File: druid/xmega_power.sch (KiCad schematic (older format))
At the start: 30 parts, among them U4 XC6206P332MR

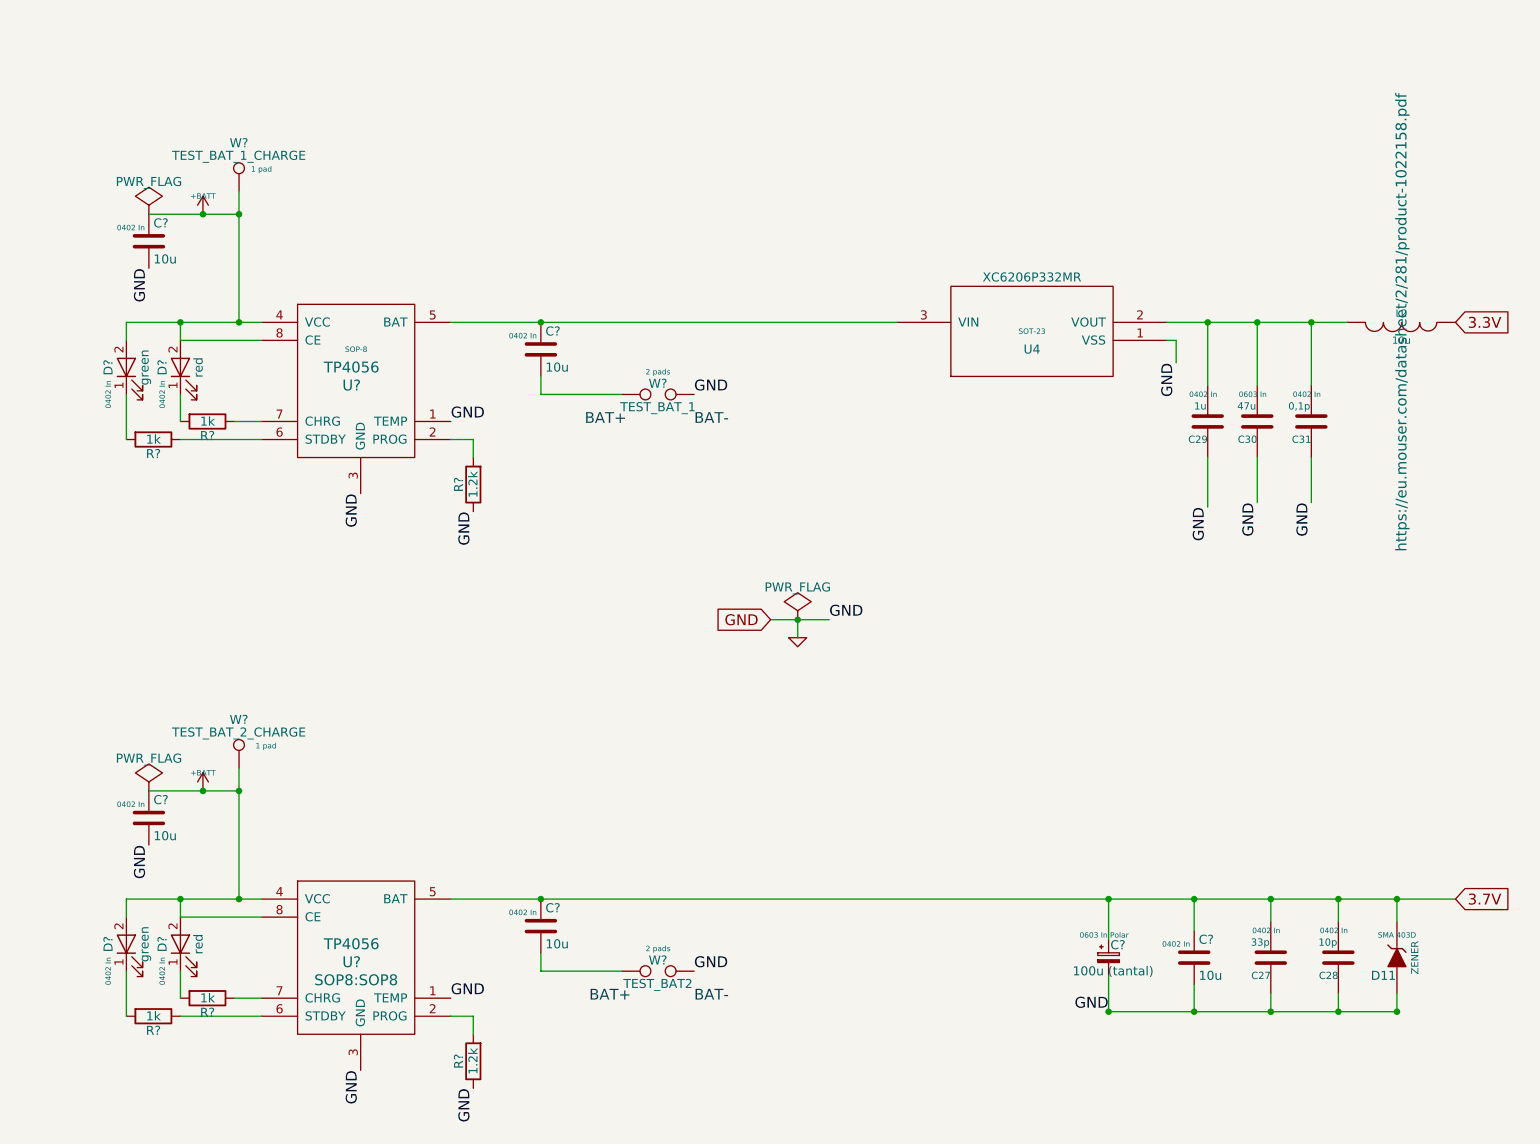
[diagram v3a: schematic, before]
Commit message: Add packages: power module completed. Add packages: keyboard module completed.
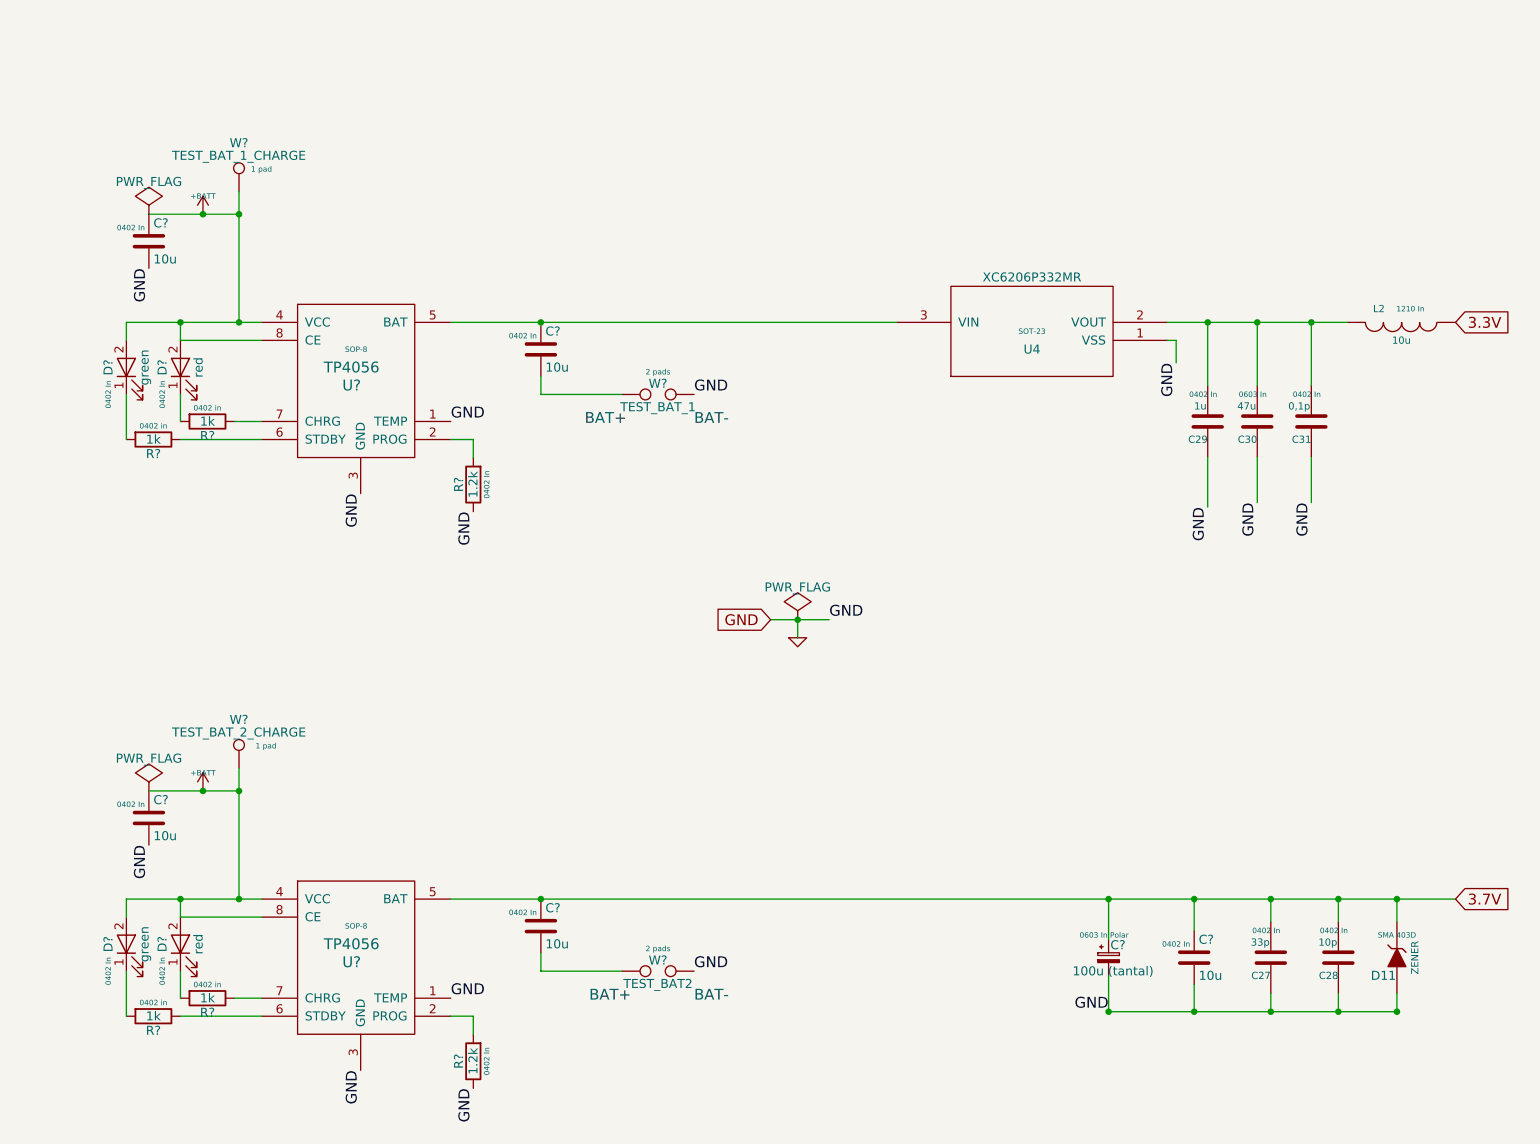
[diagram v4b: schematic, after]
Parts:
- removed R? (x3): 1k, symbol R
- removed R?: 1.2k, symbol R
- removed U?: TP4056, SOP8:SOP8, symbol TP4056
- added R? (x3): 1k, Resistors_SMD:R_0402, symbol R
- added R?: 1.2k, Resistors_SMD:R_0402, symbol R
- added U?: TP4056, SOP8:SOP8, symbol TP4056
- L2: footprint (none) -> inductor_1210_In:I_1210; case (none) -> 1210 In
- R?: footprint (none) -> Resistors_SMD:R_0402; case (none) -> 0402 in; example (none) -> https://eu.mouser.com/ProductDetail/Vishay/CRCW04021K00FKED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
- R?: footprint (none) -> Resistors_SMD:R_0402; case (none) -> 0402 In; example (none) -> https://eu.mouser.com/ProductDetail/Vishay/CRCW04021K20FKED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
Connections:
- net +BATT: now also U?.4 (VCC), U?.8 (CE)
- net 3.7V: now also U?.5 (BAT)
- net GND: now also R?.1, U?.1 (TEMP), U?.3 (GND)
- net at U?.7 (CHRG): now also R?.1
- net at D?.1 (K): now also R?.2 (x3)
- new net: R?.1, U?.6 (STDBY)
- new net: R?.1, U?.7 (CHRG)
- new net: R?.2, U?.2 (PROG)
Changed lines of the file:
@@
 U 1 1 5A9FD1C0
 P 9100 2050
-F 0 "L2" V 9050 2050 40  0000 C CNN
+F 0 "L2" V 9025 1925 40  0000 C CNN
 F 1 "10u" V 9200 2050 40  0000 C CNN
-F 2 "" H 9100 2050 60  0000 C CNN
-F 3 "https://eu.mouser.com/datasheet/2/281/product-1022158.pdf" H 9100 2050 60  0000 C CNN
+F 2 "inductor_1210_In:I_1210" H 9100 2050 60  0001 C CNN
+F 3 "https://eu.mouser.com/datasheet/2/281/product-1022158.pdf" H 9100 2050 60  0001 C CNN
 F 4 "https://eu.mouser.com/ProductDetail/Murata-Electronics/1276AS-H-100M%3dP2?qs=sGAEpiMZZMsg%252by3WlYCkUwoncuxJKc7T%2ffTlu7eSjNI%3d" V 9100 2050 60  0001 C CNN "example"
+F 5 "1210 In" V 9025 2100 30  0000 C CNN "case"
 	1    9100 2050
 	0    1    1    0
@@
 $Comp
 L R R?
-U 1 1 5C6AAFC7
-P 2475 2600
-F 0 "R?" V 2555 2600 50  0000 C CNN
-F 1 "1k" V 2475 2600 50  0000 C CNN
-F 2 "" V 2405 2600 50  0000 C CNN
-F 3 "" H 2475 2600 50  0000 C CNN
-	1    2475 2600
-	0    1    1    0
-$EndComp
-$Comp
-L R R?
 U 1 1 5C6AB0B6
 P 2175 2700
 F 0 "R?" V 2255 2700 50  0000 C CNN
 F 1 "1k" V 2175 2700 50  0000 C CNN
-F 2 "" V 2105 2700 50  0000 C CNN
-F 3 "" H 2175 2700 50  0000 C CNN
+F 2 "Resistors_SMD:R_0402" V 2105 2700 50  0001 C CNN
+F 3 "https://eu.mouser.com/datasheet/2/427/crcwce3-1223726.pdf" H 2175 2700 50  0001 C CNN
+F 4 "https://eu.mouser.com/ProductDetail/Vishay/CRCW04021K00FKEDC?qs=sGAEpiMZZMtlubZbdhIBIIZe04wfiaJWtbhT4BxhiTc%3d" V 2175 2700 60  0001 C CNN "example"
+F 5 "0402 in" V 2100 2700 30  0000 C CNN "case"
 	1    2175 2700
 	0    1    1    0
@@
 F 0 "R?" V 4030 2950 50  0000 C CNN
 F 1 "1.2k" V 3950 2950 50  0000 C CNN
-F 2 "" V 3880 2950 50  0000 C CNN
-F 3 "" H 3950 2950 50  0000 C CNN
+F 2 "Resistors_SMD:R_0402" V 3880 2950 50  0001 C CNN
+F 3 "https://eu.mouser.com/datasheet/2/427/crcwce3-1223726.pdf" H 3950 2950 50  0001 C CNN
+F 4 "https://eu.mouser.com/ProductDetail/Vishay/CRCW04021K20FKEDC?qs=sGAEpiMZZMtlubZbdhIBIIZe04wfiaJWRBT%2frAKZHAM%3d" V 3950 2950 60  0001 C CNN "example"
+F 5 "0402 In" V 3875 2950 30  0000 C CNN "case"
 	1    3950 2950
 	-1   0    0    1
@@
 $EndComp
 Connection ~ 4325 5250
-$Comp
-L TP4056 U?
-U 1 1 5C6B090F
-P 3325 5450
-F 0 "U?" H 3275 5300 60  0000 C CNN
-F 1 "TP4056" H 3275 5400 60  0000 C CNN
-F 2 "SOP8:SOP8" H 3300 5200 60  0000 C CNN
-F 3 "" H 3375 5450 60  0000 C CNN
-	1    3325 5450
-	1    0    0    -1
-$EndComp
 Text Label 3825 5800 0    60   ~ 0
 GND
@@
 Text Notes 4825 5825 2    60   ~ 0
 BAT+\n
-$Comp
-L R R?
-U 1 1 5C6B092E
-P 2475 5800
-F 0 "R?" V 2555 5800 50  0000 C CNN
-F 1 "1k" V 2475 5800 50  0000 C CNN
-F 2 "" V 2405 5800 50  0000 C CNN
-F 3 "" H 2475 5800 50  0000 C CNN
-	1    2475 5800
-	0    1    1    0
-$EndComp
-$Comp
-L R R?
-U 1 1 5C6B0934
-P 2175 5900
-F 0 "R?" V 2255 5900 50  0000 C CNN
-F 1 "1k" V 2175 5900 50  0000 C CNN
-F 2 "" V 2105 5900 50  0000 C CNN
-F 3 "" H 2175 5900 50  0000 C CNN
-	1    2175 5900
-	0    1    1    0
-$EndComp
 Wire Wire Line
 	2325 5350 2775 5350
@@
 Text Label 3325 6200 3    60   ~ 0
 GND
-$Comp
-L R R?
-U 1 1 5C6B095B
-P 3950 6150
-F 0 "R?" V 4030 6150 50  0000 C CNN
-F 1 "1.2k" V 3950 6150 50  0000 C CNN
-F 2 "" V 3880 6150 50  0000 C CNN
-F 3 "" H 3950 6150 50  0000 C CNN
-	1    3950 6150
-	-1   0    0    1
-$EndComp
 Text Label 3950 6300 3    60   ~ 0
 GND
@@
 	1    0    0    -1
 $EndComp
+$Comp
+L R R?
+U 1 1 5C6E4482
+P 2475 2600
+F 0 "R?" V 2555 2600 50  0000 C CNN
+F 1 "1k" V 2475 2600 50  0000 C CNN
+F 2 "Resistors_SMD:R_0402" V 2405 2600 50  0001 C CNN
+F 3 "https://eu.mouser.com/datasheet/2/427/crcwce3-1223726.pdf" H 2475 2600 50  0001 C CNN
+F 4 "https://eu.mouser.com/ProductDetail/Vishay/CRCW04021K00FKEDC?qs=sGAEpiMZZMtlubZbdhIBIIZe04wfiaJWtbhT4BxhiTc%3d" V 2475 2600 60  0001 C CNN "example"
+F 5 "0402 in" V 2400 2600 30  0000 C CNN "case"
+	1    2475 2600
+	0    1    1    0
+$EndComp
+$Comp
+L R R?
+U 1 1 5C6E463E
+P 2175 5900
+F 0 "R?" V 2255 5900 50  0000 C CNN
+F 1 "1k" V 2175 5900 50  0000 C CNN
+F 2 "Resistors_SMD:R_0402" V 2105 5900 50  0001 C CNN
+F 3 "https://eu.mouser.com/datasheet/2/427/crcwce3-1223726.pdf" H 2175 5900 50  0001 C CNN
+F 4 "https://eu.mouser.com/ProductDetail/Vishay/CRCW04021K00FKEDC?qs=sGAEpiMZZMtlubZbdhIBIIZe04wfiaJWtbhT4BxhiTc%3d" V 2175 5900 60  0001 C CNN "example"
+F 5 "0402 in" V 2100 5900 30  0000 C CNN "case"
+	1    2175 5900
+	0    1    1    0
+$EndComp
+$Comp
+L R R?
+U 1 1 5C6E49C1
+P 2475 5800
+F 0 "R?" V 2555 5800 50  0000 C CNN
+F 1 "1k" V 2475 5800 50  0000 C CNN
+F 2 "Resistors_SMD:R_0402" V 2405 5800 50  0001 C CNN
+F 3 "https://eu.mouser.com/datasheet/2/427/crcwce3-1223726.pdf" H 2475 5800 50  0001 C CNN
+F 4 "https://eu.mouser.com/ProductDetail/Vishay/CRCW04021K00FKEDC?qs=sGAEpiMZZMtlubZbdhIBIIZe04wfiaJWtbhT4BxhiTc%3d" V 2475 5800 60  0001 C CNN "example"
+F 5 "0402 in" V 2400 5800 30  0000 C CNN "case"
+	1    2475 5800
+	0    1    1    0
+$EndComp
+$Comp
+L R R?
+U 1 1 5C6E5065
+P 3950 6150
+F 0 "R?" V 4030 6150 50  0000 C CNN
+F 1 "1.2k" V 3950 6150 50  0000 C CNN
+F 2 "Resistors_SMD:R_0402" V 3880 6150 50  0001 C CNN
+F 3 "https://eu.mouser.com/datasheet/2/427/crcwce3-1223726.pdf" H 3950 6150 50  0001 C CNN
+F 4 "https://eu.mouser.com/ProductDetail/Vishay/CRCW04021K20FKEDC?qs=sGAEpiMZZMtlubZbdhIBIIZe04wfiaJWRBT%2frAKZHAM%3d" V 3950 6150 60  0001 C CNN "example"
+F 5 "0402 In" V 3875 6150 30  0000 C CNN "case"
+	1    3950 6150
+	-1   0    0    1
+$EndComp
+$Comp
+L TP4056 U?
+U 1 1 5C6E5C3E
+P 3325 5450
+F 0 "U?" H 3275 5300 60  0000 C CNN
+F 1 "TP4056" H 3275 5400 60  0000 C CNN
+F 2 "SOP8:SOP8" H 3300 5200 60  0001 C CNN
+F 3 "https://dlnmh9ip6v2uc.cloudfront.net/datasheets/Prototyping/TP4056.pdf" H 3375 5450 60  0001 C CNN
+F 4 "SOP-8" H 3300 5500 30  0000 C CNN "case"
+F 5 "https://ru.aliexpress.com/item/20-TP4056-TP4056/32965308715.html?spm=a2g0v.search0604.3.19.3b7342ceZ2YQqe&s=p&ws_ab_test=searchweb0_0%2Csearchweb201602_6_10065_10068_319_317_10696_10084_453_10083_454_10618_10304_10307_10820_10821_10301_537_536_10902_10843_10059_10884_10887_321_322_10103%2Csearchweb201603_51%2CppcSwitch_0&algo_pvid=d8dbfd72-123f-4196-8109-e7e6d3afca91&algo_expid=d8dbfd72-123f-4196-8109-e7e6d3afca91-2" H 3325 5450 60  0001 C CNN "example"
+	1    3325 5450
+	1    0    0    -1
+$EndComp

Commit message: move to kicad 5
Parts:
- C27, C28, C29, C30, C31: symbol C-RESCUE-xmobile -> xmobile-rescue:C-RESCUE-xmobile
- C? (x5): symbol C -> xmobile-rescue:C
- C?: symbol CP_Small -> xmobile-rescue:CP_Small
- D11: symbol ZENER-RESCUE-xmobile -> xmobile-rescue:ZENER-RESCUE-xmobile
- D? (x4): symbol LED-RESCUE-xmobile -> xmobile-rescue:LED-RESCUE-xmobile
- L2: symbol INDUCTOR -> xmobile-rescue:INDUCTOR
- R? (x6): symbol R -> xmobile-rescue:R
- U4: symbol XC6206P332MR -> xmobile-rescue:XC6206P332MR
- U? (x2): symbol TP4056 -> xmobile-rescue:TP4056
- W? (x2): symbol TEST-RESCUE-xmobile -> xmobile-rescue:TEST-RESCUE-xmobile
- W? (x2): symbol TEST_1P -> xmobile-rescue:TEST_1P
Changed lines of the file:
@@
-EESchema Schematic File Version 2
-LIBS:xmobile-rescue
-LIBS:power
-LIBS:device
-LIBS:transistors
-LIBS:conn
-LIBS:linear
-LIBS:regul
-LIBS:74xx
-LIBS:cmos4000
-LIBS:adc-dac
-LIBS:memory
-LIBS:xilinx
-LIBS:microcontrollers
-LIBS:dsp
-LIBS:microchip
-LIBS:analog_switches
-LIBS:motorola
-LIBS:texas
-LIBS:intel
-LIBS:audio
-LIBS:interface
-LIBS:digital-audio
-LIBS:philips
-LIBS:display
-LIBS:cypress
-LIBS:siliconi
-LIBS:opto
-LIBS:atmel
-LIBS:contrib
-LIBS:valves
-LIBS:XC6206P332MR
-LIBS:STF202-22T1G
-LIBS:MCP73871
-LIBS:switch1
-LIBS:SRAM
-LIBS:xmega128a1u_bga100
-LIBS:sim-holders
-LIBS:max7370
-LIBS:tp4056
+EESchema Schematic File Version 4
 LIBS:xmobile-cache
-EELAYER 25 0
+EELAYER 26 0
 EELAYER END
 $Descr A4 11693 8268
@@
 $EndDescr
 $Comp
-L INDUCTOR L2
+L xmobile-rescue:INDUCTOR L2
 U 1 1 5A9FD1C0
 P 9100 2050
@@
 $EndComp
 $Comp
-L C-RESCUE-xmobile C31
+L xmobile-rescue:C-RESCUE-xmobile C31
 U 1 1 5A9FD1C7
 P 8600 2600
@@
 $EndComp
 $Comp
-L C-RESCUE-xmobile C30
+L xmobile-rescue:C-RESCUE-xmobile C30
 U 1 1 5A9FD1CE
 P 8300 2600
@@
 $EndComp
 $Comp
-L C-RESCUE-xmobile C29
+L xmobile-rescue:C-RESCUE-xmobile C29
 U 1 1 5A9FD1D5
 P 8025 2600
@@
 $EndComp
 $Comp
-L GND-RESCUE-xmobile #PWR04
+L xmobile-rescue:GND-RESCUE-xmobile #PWR04
 U 1 1 5A9FD1E3
 P 5750 3800
@@
 $EndComp
 $Comp
-L C-RESCUE-xmobile C27
+L xmobile-rescue:C-RESCUE-xmobile C27
 U 1 1 5A9FD1F7
 P 8375 5575
@@
 $EndComp
 $Comp
-L C-RESCUE-xmobile C28
+L xmobile-rescue:C-RESCUE-xmobile C28
 U 1 1 5A9FD1FE
 P 8750 5575
@@
 $EndComp
 $Comp
-L XC6206P332MR U4
+L xmobile-rescue:XC6206P332MR U4
 U 1 1 5A9FD205
 P 7050 2100
@@
 GND
 $Comp
-L ZENER-RESCUE-xmobile D11
+L xmobile-rescue:ZENER-RESCUE-xmobile D11
 U 1 1 5A9FD218
 P 9075 5575
@@
 Connection ~ 9075 5250
 $Comp
-L +BATT #PWR05
+L xmobile-rescue:+BATT #PWR05
 U 1 1 5A9FE80A
 P 2450 1450
@@
 Connection ~ 4325 2050
 $Comp
-L PWR_FLAG #FLG06
+L xmobile-rescue:PWR_FLAG #FLG06
 U 1 1 5AB7534F
 P 2150 4650
@@
 $EndComp
 $Comp
-L PWR_FLAG #FLG07
+L xmobile-rescue:PWR_FLAG #FLG07
 U 1 1 5AB75478
 P 5750 3700
@@
 3.7V
 $Comp
-L TP4056 U?
+L xmobile-rescue:TP4056 U?
 U 1 1 5C6A7D13
 P 3325 2250
@@
 BAT+\n
 $Comp
-L LED-RESCUE-xmobile D?
+L xmobile-rescue:LED-RESCUE-xmobile D?
 U 1 1 5C6AA662
 P 2325 2300
@@
 $EndComp
 $Comp
-L LED-RESCUE-xmobile D?
+L xmobile-rescue:LED-RESCUE-xmobile D?
 U 1 1 5C6AA7C8
 P 2025 2300
@@
 $EndComp
 $Comp
-L R R?
+L xmobile-rescue:R R?
 U 1 1 5C6AB0B6
 P 2175 2700
@@
 Connection ~ 2325 2050
 $Comp
-L C C?
+L xmobile-rescue:C C?
 U 1 1 5C6AB784
 P 2150 1600
@@
 GND
 $Comp
-L R R?
+L xmobile-rescue:R R?
 U 1 1 5C6AC8FB
 P 3950 2950
@@
 	7475 5875 9075 5875
 $Comp
-L +BATT #PWR?
+L xmobile-rescue:+BATT #PWR?
 U 1 1 5C6B0901
 P 2450 4650
@@
 Connection ~ 2450 4650
 $Comp
-L PWR_FLAG #FLG?
+L xmobile-rescue:PWR_FLAG #FLG?
 U 1 1 5C6B204A
 P 2150 1450
@@
 $EndComp
 $Comp
-L TEST-RESCUE-xmobile W?
+L xmobile-rescue:TEST-RESCUE-xmobile W?
 U 1 1 5C6B9CD1
 P 4975 2450
@@
 $EndComp
 $Comp
-L TEST-RESCUE-xmobile W?
+L xmobile-rescue:TEST-RESCUE-xmobile W?
 U 1 1 5C6BA4AE
 P 4975 5650
@@
 $EndComp
 $Comp
-L TEST_1P W?
+L xmobile-rescue:TEST_1P W?
 U 1 1 5C6C9437
 P 2650 1325
@@
 Connection ~ 2650 1450
 $Comp
-L TEST_1P W?
+L xmobile-rescue:TEST_1P W?
 U 1 1 5C6C9C6E
 P 2650 4525
@@
 Connection ~ 2650 4650
 $Comp
-L LED-RESCUE-xmobile D?
+L xmobile-rescue:LED-RESCUE-xmobile D?
 U 1 1 5C6CA596
 P 2025 5500
@@
 $EndComp
 $Comp
-L LED-RESCUE-xmobile D?
+L xmobile-rescue:LED-RESCUE-xmobile D?
 U 1 1 5C6CB16E
 P 2325 5500
@@
 $EndComp
 $Comp
-L C C?
+L xmobile-rescue:C C?
 U 1 1 5C6D036E
 P 2150 4800
@@
 $EndComp
 $Comp
-L C C?
+L xmobile-rescue:C C?
 U 1 1 5C6D0763
 P 4325 5400
@@
 $EndComp
 $Comp
-L C C?
+L xmobile-rescue:C C?
 U 1 1 5C6D0925
 P 4325 2200
@@
 $EndComp
 $Comp
-L C C?
+L xmobile-rescue:C C?
 U 1 1 5C6D24E8
 P 7950 5575
@@
 $EndComp
 $Comp
-L CP_Small C?
+L xmobile-rescue:CP_Small C?
 U 1 1 5C6D2D36
 P 7475 5575
@@
 $EndComp
 $Comp
-L R R?
+L xmobile-rescue:R R?
 U 1 1 5C6E4482
 P 2475 2600
@@
 $EndComp
 $Comp
-L R R?
+L xmobile-rescue:R R?
 U 1 1 5C6E463E
 P 2175 5900
@@
 $EndComp
 $Comp
-L R R?
+L xmobile-rescue:R R?
 U 1 1 5C6E49C1
 P 2475 5800
@@
 $EndComp
 $Comp
-L R R?
+L xmobile-rescue:R R?
 U 1 1 5C6E5065
 P 3950 6150
@@
 $EndComp
 $Comp
-L TP4056 U?
+L xmobile-rescue:TP4056 U?
 U 1 1 5C6E5C3E
 P 3325 5450

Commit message: looks like all packages added.
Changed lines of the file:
@@
 $EndComp
 Wire Wire Line
-	7800 2050 8800 2050
+	7800 2050 8025 2050
 Wire Wire Line
 	8600 3050 8600 2800
@@
 	5750 3800 5750 3700
 Wire Wire Line
-	5600 3700 5925 3700
+	5600 3700 5750 3700
 Wire Wire Line
 	8025 2050 8025 2400
@@
 	8600 2400 8600 2050
 Wire Wire Line
-	3825 5250 9400 5250
+	3825 5250 4325 5250
 Wire Wire Line
 	7475 5675 7475 5875
-Connection ~ 7475 5875
 Wire Wire Line
 	7950 5725 7950 5875
@@
 Wire Wire Line
 	9075 5875 9075 5775
-Connection ~ 9075 5875
 Connection ~ 9075 5250
 $Comp
@@
 $EndComp
 Wire Wire Line
-	3825 2050 6300 2050
+	3825 2050 4325 2050
 Text GLabel 5600 3700 0    60   Input ~ 0
 GND
@@
 	2025 2700 2025 2450
 Wire Wire Line
-	2025 2050 2775 2050
+	2025 2050 2325 2050
 Wire Wire Line
 	2025 2050 2025 2150
@@
 GND
 Wire Wire Line
-	2150 1450 2650 1450
-Wire Wire Line
-	2650 1325 2650 2050
+	2150 1450 2450 1450
+Wire Wire Line
+	2650 1325 2650 1450
 Connection ~ 2650 2050
 Text Label 3325 3000 3    60   ~ 0
@@
 Connection ~ 2450 1450
 Wire Wire Line
-	7475 5875 9075 5875
+	7475 5875 7950 5875
 $Comp
 L xmobile-rescue:+BATT #PWR?
@@
 	2025 5900 2025 5650
 Wire Wire Line
-	2025 5250 2775 5250
+	2025 5250 2325 5250
 Wire Wire Line
 	2025 5250 2025 5350
@@
 GND
 Wire Wire Line
-	2150 4650 2650 4650
-Wire Wire Line
-	2650 4525 2650 5250
+	2150 4650 2450 4650
+Wire Wire Line
+	2650 4525 2650 4650
 Connection ~ 2650 5250
 Text Label 3325 6200 3    60   ~ 0
@@
 	1    0    0    -1
 $EndComp
+Wire Wire Line
+	8300 2050 8600 2050
+Wire Wire Line
+	8600 2050 8800 2050
+Wire Wire Line
+	8025 2050 8300 2050
+Wire Wire Line
+	7950 5875 8375 5875
+Wire Wire Line
+	8375 5875 8750 5875
+Wire Wire Line
+	8750 5875 9075 5875
+Wire Wire Line
+	7475 5250 7950 5250
+Wire Wire Line
+	7950 5250 8375 5250
+Wire Wire Line
+	8375 5250 8750 5250
+Wire Wire Line
+	8750 5250 9075 5250
+Wire Wire Line
+	9075 5250 9400 5250
+Wire Wire Line
+	5750 3700 5925 3700
+Wire Wire Line
+	4325 2050 6300 2050
+Wire Wire Line
+	2325 2050 2650 2050
+Wire Wire Line
+	2650 2050 2775 2050
+Wire Wire Line
+	2450 1450 2650 1450
+Wire Wire Line
+	4325 5250 7475 5250
+Wire Wire Line
+	2325 5250 2650 5250
+Wire Wire Line
+	2650 5250 2775 5250
+Wire Wire Line
+	2450 4650 2650 4650
+Wire Wire Line
+	2650 1450 2650 2050
+Wire Wire Line
+	2650 4650 2650 5250
 $EndSCHEMATC

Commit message: remove electric  warnings and errors. annotate elements. fix microUSB-B symbol.
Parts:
- gave numbers to parts that had none: 22
- renumbered C29 to C27, C30 to C28, C27 to C29, C31 to C30, C28 to C31, D11 to D13, L2 to L1, U4 to U5
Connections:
- net +BATT: no longer names the net of C21.1, D11.2 (A), D9.2 (A), U3.4 (VCC), U3.8 (CE), W5.1
- net +BATT: no longer C22.1, D10.2 (A), D12.2 (A), U4.4 (VCC), U4.8 (CE), W6.1
- new net: C22.1, D10.2 (A), D12.2 (A), U4.4 (VCC), U4.8 (CE), W6.1
